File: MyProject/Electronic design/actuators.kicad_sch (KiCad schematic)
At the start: 5 parts

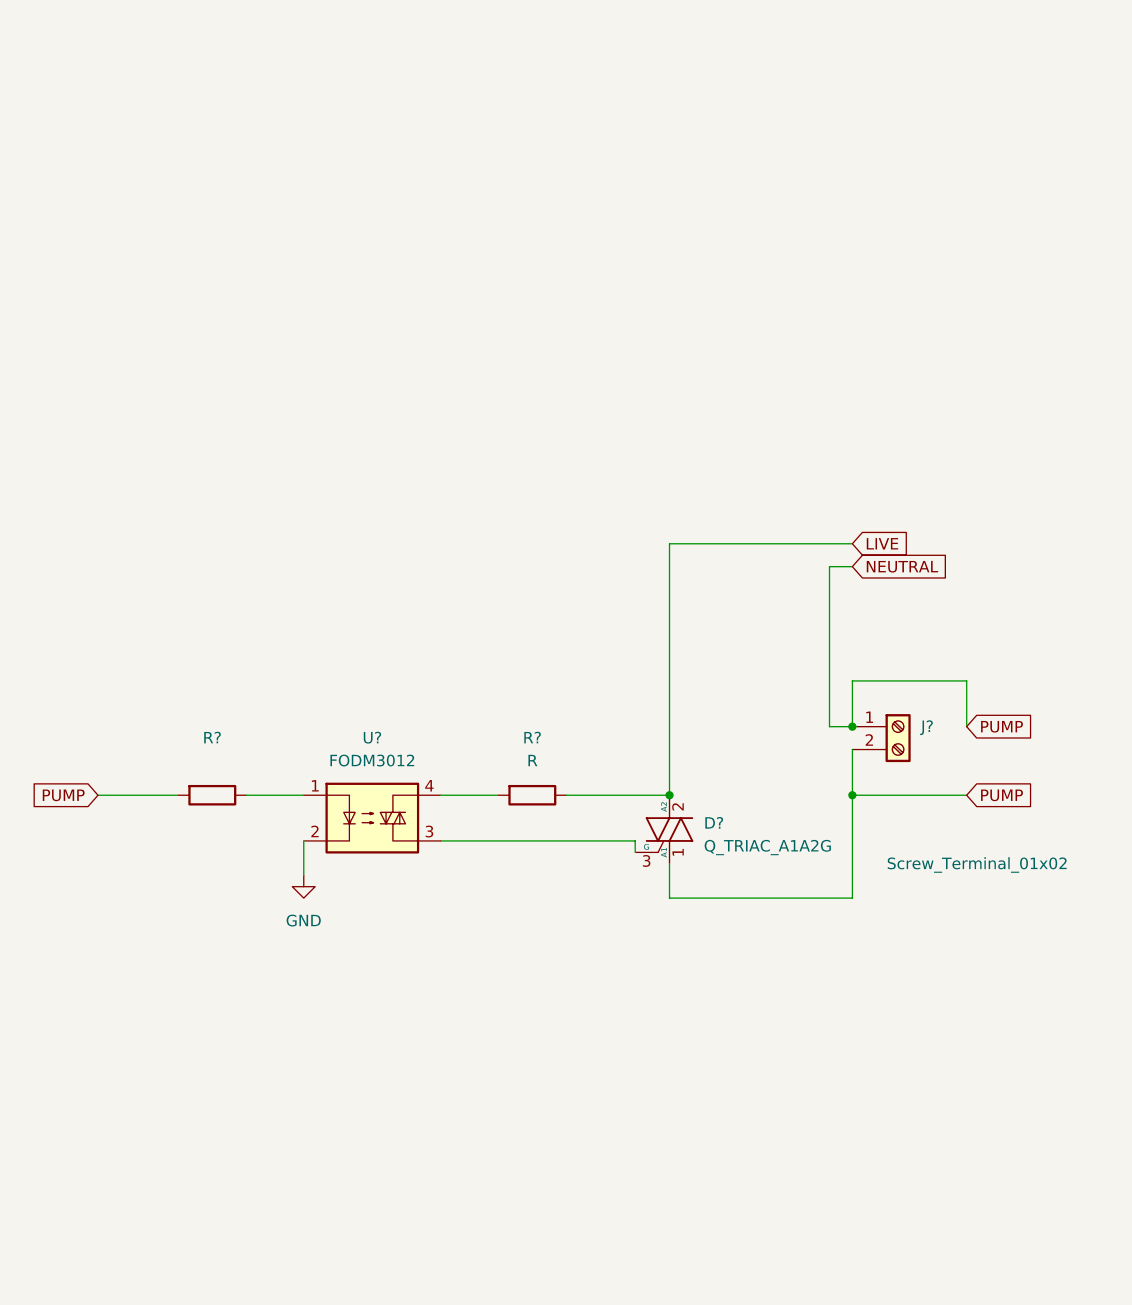
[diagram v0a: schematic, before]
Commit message: Shortening file names for Windows users
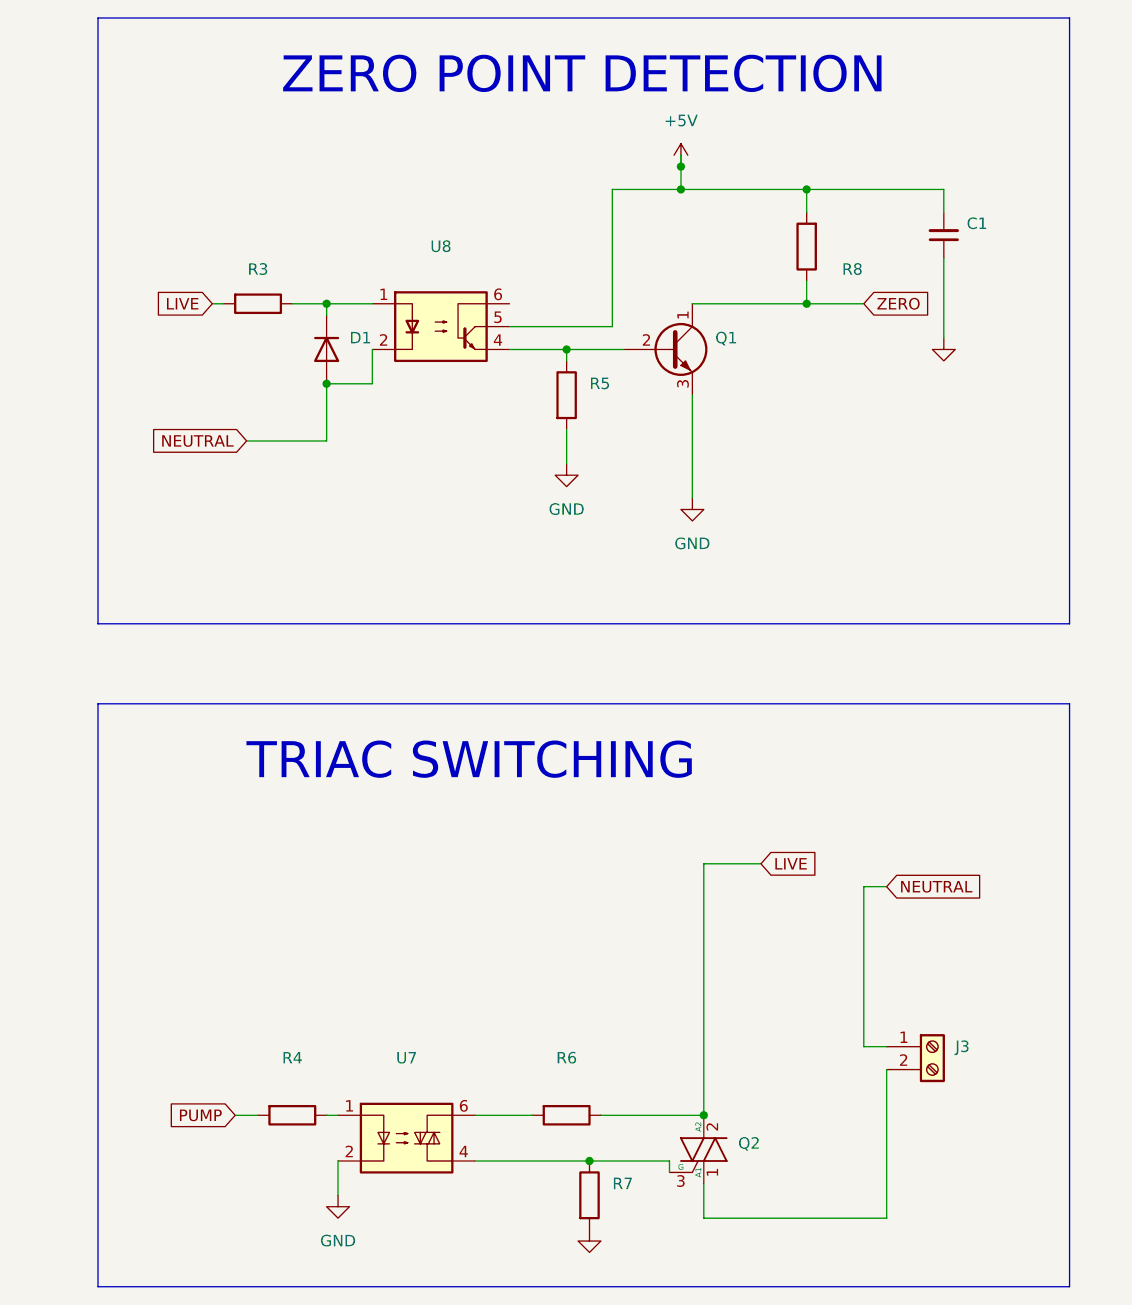
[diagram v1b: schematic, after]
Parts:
- removed D?: Q_TRIAC_A1A2G, symbol Device:Q_TRIAC_A1A2G
- removed U?: FODM3012, Package_DIP:SMDIP-4_W7.62mm, symbol Relay_SolidState:FODM3012
- added C1: (no value), symbol Device:C_Small
- added D1: (no value), symbol Simulation_SPICE:DIODE
- added Q1: (no value), symbol Transistor_BJT:BC547
- added Q2: (no value), symbol Triac_Thyristor:BT136-500
- added R3, R5, R7, R8: (no value), symbol Device:R
- added U7: (no value), symbol Relay_SolidState:MOC3021M
- added U8: (no value), symbol Isolator:4N35
- J3: renamed from J?; value Screw_Terminal_01x02 -> (none)
- R4: renamed from R?; value ~ -> (none)
- R6: renamed from R?; value R -> (none)
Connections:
- net GND: now also C1.1, Q1.3 (E), R5.2, R7.2, U7.2
- net LIVE: now also Q2.2 (A2), R3.2
- net NEUTRAL: now also D1.1 (A), U8.2; no longer J3.2 (Pin_2), R4.2
- net at R4.1: now also U7.1
- net at R6.2: now also U7.6
- new net: D1.2 (K), R3.1, U8.1
- new net: Q1.2 (B), R5.1, U8.4
- new net: J3.2 (Pin_2), Q2.1 (A1)
- new net: Q2.3 (G), R7.1, U7.4
- new net +5V: C1.2, R8.2, U8.5
- new net PUMP: R4.2
- new net ZERO: Q1.1 (C), R8.1
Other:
- note added: "TRIAC SWITCHING"
- note added: "ZERO POINT DETECTION"
- moved on the sheet: J3, R4, R6
